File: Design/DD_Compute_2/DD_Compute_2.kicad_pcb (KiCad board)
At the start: 4 copper layers, 200 x 65 mm, 183 parts, among them J1 DISP. BOARD CONN 1 (1-20), J10 DISP_BOARD_CONN_3, J11 ISOLATED OUPTUTS & POWER, J12 ISOLATED INPUTS, J13 ODOMETER MODULE, J14 CAR INTERFACE - 0349610341, J15 SWD, J2 DISP. BOARD CONN 2 (21-40), J3 TRIP BOARD CONN 1 (1-10), J4 TRIP BOARD CONN 2 (11-22), J5 Conn_01x03, J6 Conn_01x03, J7 Conn_01x03, J8 POWER SUPPLY - 0349580340, J9 CAR INTERFACE - 0349610341 - 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, U1 74HCT00D,653, U10 SN74LV1T34DCK, U13 VO0631T, U16 VO0631T, U17 SRV05-4, U18 25LC020AT-E/SN, U19 TJR1443, U2 74HCT244D,653, U20 STM32F103V8Tx, U21 74HC165D-Q100,118, U22 74HC165D-Q100,118, U23 74HC165D-Q100,118, U24 SRV05-4, U25 SRV05-4, U26 SRV05-4, U27 SRV05-4, U28 SRV05-4, U29 SRV05-4, U3 74HCT244D,653, U30 LMV324AIDR, U31 LMV324AIDR, U4 74HC165D-Q100,118, U5 SN74LV1T34DCK, U6 74HCT244D,653, U7 74HCT244D,653, U9 SN74LV1T34DCK, Y1 8MHz

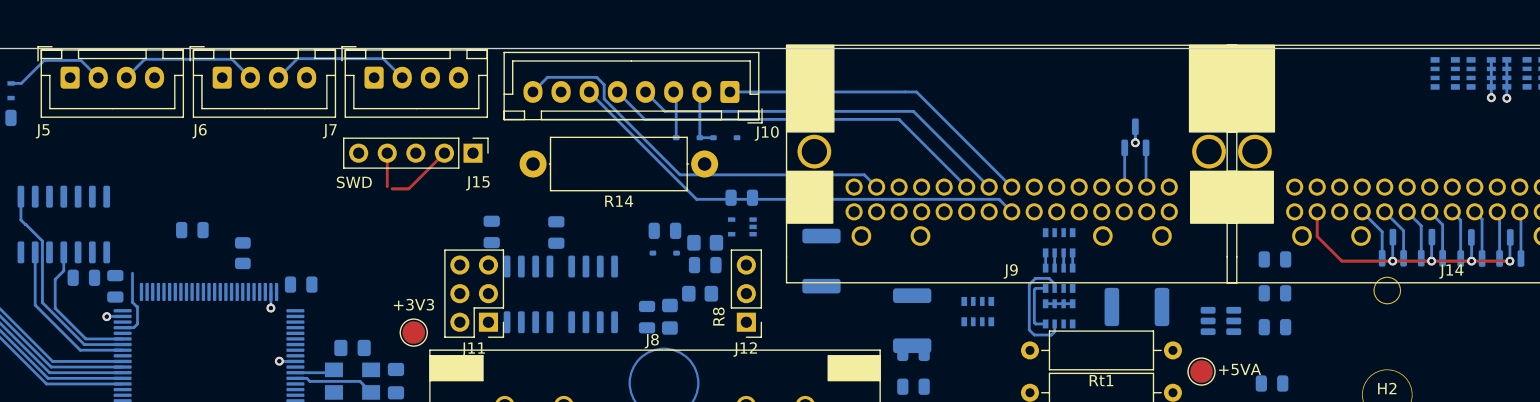
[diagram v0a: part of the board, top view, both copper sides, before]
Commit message: warning module update; ws2812->ws2813 (backup data in)
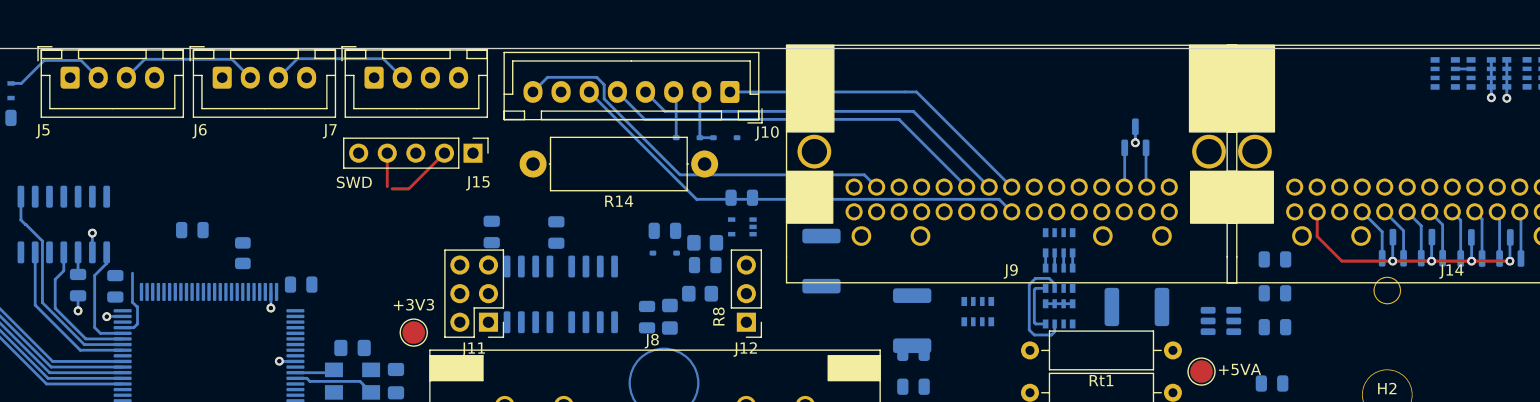
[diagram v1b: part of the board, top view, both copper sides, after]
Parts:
- moved C43 0.83 mm to (135.7, 94.8), turned to -90 degrees
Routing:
- net /CAN_TX: track 0.00 -> 9.82 mm
- net GND: track 63.0 -> 66.0 mm, vias 28 -> 30
- net +5V: track 9.54 -> 11.5 mm
- net Net-(RN13-R2.2): track 0.00 -> 1.40 mm
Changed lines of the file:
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@@
   )
   (footprint "Capacitor_SMD:C_0805_2012Metric" (layer "B.Cu")
-    (at 136.199 94.1386)
+    (at 135.6868 94.7928 -90)
     (descr "Capacitor SMD 0805 (2012 Metric), square (rectangular) end terminal, IPC_7351 nominal, (Body size source: IPC-SM-782 page 76, https://www.pcb-3d.com/wordpress/wp-content/uploads/ipc-sm-782a_amendment_1_and_2.pdf, https://docs.google.com/spreadsheets/d/1BsfQQcO9C6DZCsRaXUlFlo91Tg2WpOkGARC1WS5S8t0/edit?usp=sharing), generated with kicad-footprint-generator")
     (tags "capacitor")
@@
     (property "ki_keywords" "capacitor cap")
     (attr smd)
-    (fp_text reference "C43" (at 0 1.68) (layer "B.SilkS")
+    (fp_text reference "C43" (at 0 1.68 90) (layer "B.SilkS")
         (effects (font (size 1 1) (thickness 0.15)) (justify mirror))
     )
-    (fp_text value "100nF" (at 0 -1.68) (layer "B.Fab")
+    (fp_text value "100nF" (at 0 -1.68 90) (layer "B.Fab")
         (effects (font (size 1 1) (thickness 0.15)) (justify mirror))
     )
-    (fp_text user "${REFERENCE}" (at 0 0) (layer "B.Fab")
+    (fp_text user "${REFERENCE}" (at 0 0 90) (layer "B.Fab")
         (effects (font (size 0.5 0.5) (thickness 0.08)) (justify mirror))
     )
@@
     (fp_line (start 1 0.625) (end 1 -0.625)
       (stroke (width 0.1) (type solid)) (layer "B.Fab"))
-    (pad "1" smd roundrect (at -0.95 0) (size 1 1.45) (layers "B.Cu" "B.Paste" "B.Mask") (roundrect_rratio 0.25)
+    (pad "1" smd roundrect (at -0.95 0 270) (size 1 1.45) (layers "B.Cu" "B.Paste" "B.Mask") (roundrect_rratio 0.25)
       (net 11 "+5V") (pintype "passive"))
-    (pad "2" smd roundrect (at 0.95 0) (size 1 1.45) (layers "B.Cu" "B.Paste" "B.Mask") (roundrect_rratio 0.25)
+    (pad "2" smd roundrect (at 0.95 0 270) (size 1 1.45) (layers "B.Cu" "B.Paste" "B.Mask") (roundrect_rratio 0.25)
       (net 22 "GND") (pintype "passive"))
     (model "${KICAD6_3DMODEL_DIR}/Capacitor_SMD.3dshapes/C_0805_2012Metric.wrl"
@@
   (segment (start 141.7168 123.3068) (end 141.6812 123.3424) (width 0.25) (layer "B.Cu") (net 11))
   (segment (start 162.6872 127.2794) (end 162.6872 129.0216) (width 0.25) (layer "B.Cu") (net 11))
+  (segment (start 135.6868 91.883) (end 135.6868 93.8428) (width 0.25) (layer "B.Cu") (net 11))
   (segment (start 102.854 101.9864) (end 103.3646 101.4758) (width 1.2) (layer "F.Cu") (net 12))
   (segment (start 103.3646 101.4758) (end 116.2586 101.4758) (width 1.2) (layer "F.Cu") (net 12))
@@
   (via (at 114.1476 78.5876) (size 0.8) (drill 0.4) (layers "F.Cu" "B.Cu") (net 22))
   (via (at 118.876299 92.155499) (size 0.8) (drill 0.4) (layers "F.Cu" "B.Cu") (net 22))
+  (via (at 135.6868 97.0788) (size 0.8) (drill 0.4) (layers "F.Cu" "B.Cu") (net 22))
   (via (at 137.93 118.3174) (size 0.8) (drill 0.4) (layers "F.Cu" "B.Cu") (net 22))
   (via (at 117.7036 110.0836) (size 0.8) (drill 0.4) (layers "F.Cu" "B.Cu") (net 22))
@@
   (via (at 259.72765 121.8976) (size 0.8) (drill 0.4) (layers "F.Cu" "B.Cu") (net 22))
   (via (at 153.5684 101.5492) (size 0.8) (drill 0.4) (layers "F.Cu" "B.Cu") (net 22))
+  (via (at 136.9568 90.17) (size 0.8) (drill 0.4) (layers "F.Cu" "B.Cu") (net 22))
   (via (at 152.8144 96.829) (size 0.8) (drill 0.4) (layers "F.Cu" "B.Cu") (net 22))
   (via (at 103.3272 115.8148) (size 0.8) (drill 0.4) (layers "F.Cu" "B.Cu") (net 22))
@@
   (segment (start 139.7954 118.292) (end 137.93 118.3174) (width 0.25) (layer "B.Cu") (net 22))
   (segment (start 130.8964 125.7452) (end 130.9116 125.73) (width 0.25) (layer "B.Cu") (net 22))
+  (segment (start 135.6868 95.7428) (end 135.6868 97.0788) (width 0.25) (layer "B.Cu") (net 22))
   (segment (start 139.645 97.5732) (end 138.2526 97.5732) (width 0.25) (layer "B.Cu") (net 22))
   (segment (start 153.1872 115.8494) (end 154.6606 115.8494) (width 0.25) (layer "B.Cu") (net 22))
@@
   (segment (start 259.72765 120.1704) (end 259.72765 121.8976) (width 0.25) (layer "B.Cu") (net 22))
   (segment (start 221.642 96.444) (end 224.042 96.444) (width 0.25) (layer "B.Cu") (net 22))
+  (segment (start 136.9568 91.883) (end 136.9568 90.17) (width 0.25) (layer "B.Cu") (net 22))
   (segment (start 137.93 118.3174) (end 137.9554 118.292) (width 0.25) (layer "B.Cu") (net 22))
   (segment (start 249.26285 121.8468) (end 249.21205 121.8976) (width 0.25) (layer "B.Cu") (net 22))
@@
   (segment (start 317.904934 131.1888) (end 317.626534 130.9104) (width 0.25) (layer "B.Cu") (net 153))
   (segment (start 317.579934 134.3496) (end 317.904934 134.0246) (width 0.25) (layer "B.Cu") (net 153))
+  (segment (start 258.0416 75.5864) (end 259.4368 75.5864) (width 0.25) (layer "B.Cu") (net 154))
   (segment (start 221.642 91.9304) (end 221.642 93.28) (width 0.25) (layer "B.Cu") (net 156))
   (segment (start 311.7264 87.8044) (end 311.7264 89.2048) (width 0.25) (layer "B.Cu") (net 158))
@@
   (segment (start 156.591 127.2794) (end 157.861 126.0094) (width 0.25) (layer "B.Cu") (net 177))
   (segment (start 148.0445 118.232701) (end 147.77 118.507201) (width 0.25) (layer "B.Cu") (net 177))
+  (segment (start 137.668 99.0732) (end 137.16 98.5652) (width 0.25) (layer "B.Cu") (net 185))
+  (segment (start 139.645 99.0732) (end 137.668 99.0732) (width 0.25) (layer "B.Cu") (net 185))
+  (segment (start 137.16 98.5652) (end 137.16 93.9292) (width 0.25) (layer "B.Cu") (net 185))
+  (segment (start 137.16 93.9292) (end 138.2268 92.8624) (width 0.25) (layer "B.Cu") (net 185))
+  (segment (start 138.2268 92.8624) (end 138.2268 91.883) (width 0.25) (layer "B.Cu") (net 185))
   (segment (start 134.4168 93.5228) (end 134.4168 91.883) (width 0.25) (layer "B.Cu") (net 186))
   (segment (start 133.6548 94.2848) (end 134.4168 93.5228) (width 0.25) (layer "B.Cu") (net 186))
